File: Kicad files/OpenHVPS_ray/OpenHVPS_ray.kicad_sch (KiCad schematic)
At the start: 69 parts, among them J1 Conn_01x03_Male, J2 Conn_01x03_Male, Q1 FQT7N10, Q2 BC846A, Q3 MMDT3906, U1 MAX6008AEUR+T, U2 74HC14, U3 MAX4162, U4 CD14538BM

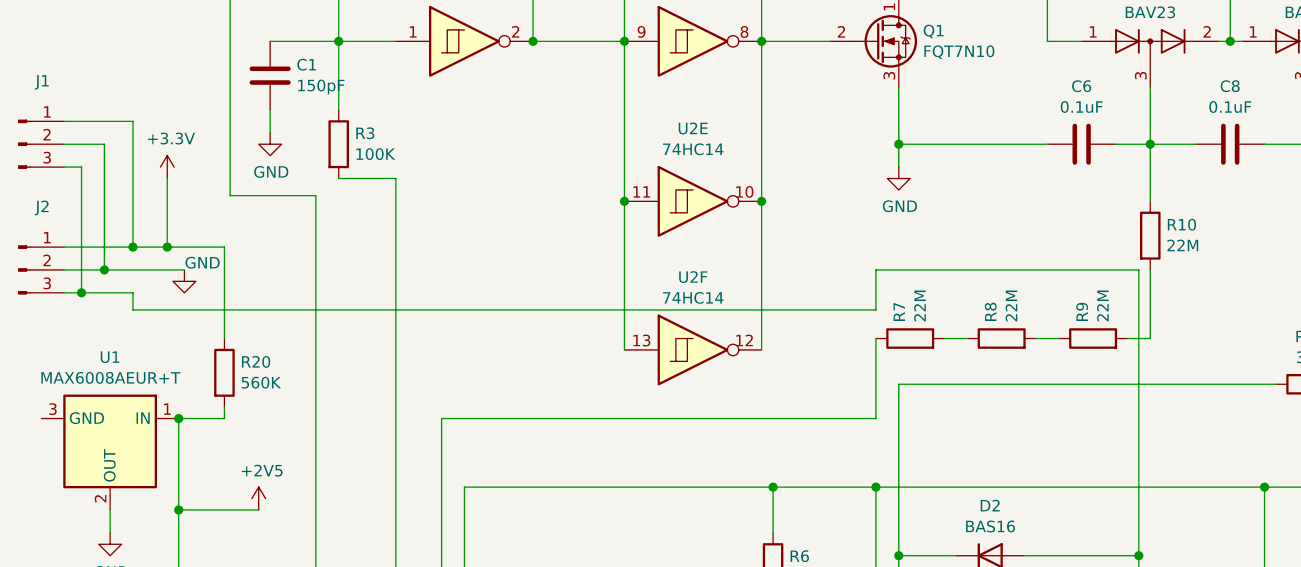
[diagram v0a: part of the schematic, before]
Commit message: Flipped R1 and +-P-GND and naming
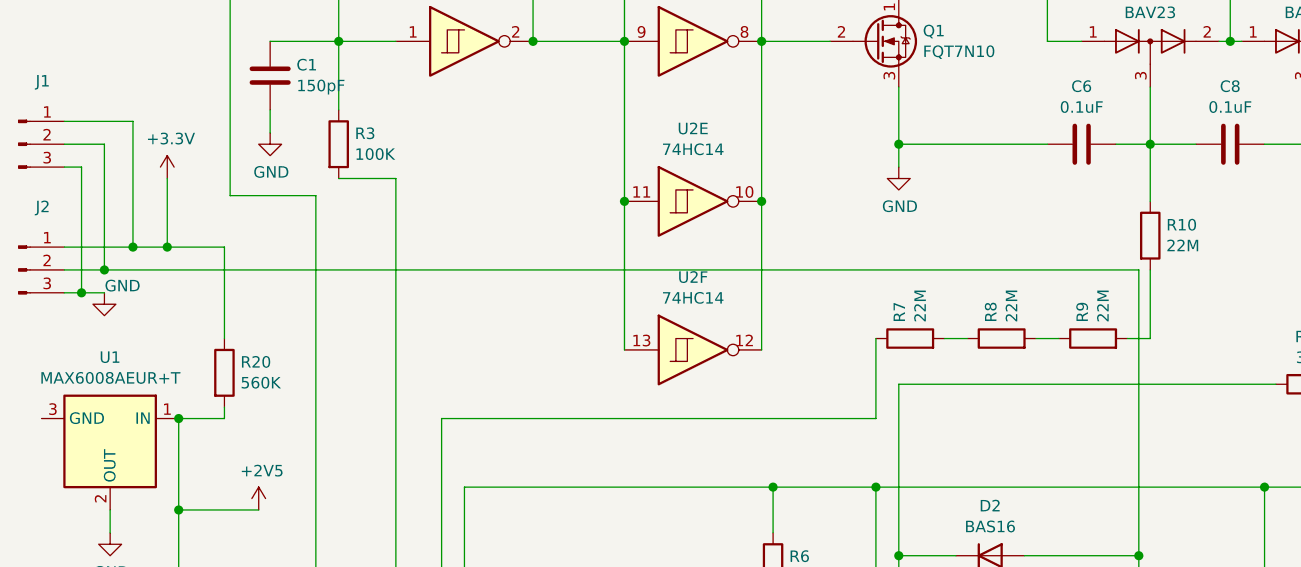
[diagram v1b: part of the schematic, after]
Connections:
- net GND: now also J1.3 (Pin_3), J2.3 (Pin_3); no longer J1.2 (Pin_2), J2.2 (Pin_2)
- net at D2.2 (A), U4.6 (Q): now also J1.2 (Pin_2), J2.2 (Pin_2); no longer J1.3 (Pin_3), J2.3 (Pin_3)
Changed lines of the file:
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@@
     (stroke (width 0) (type solid) (color 0 0 0 0))
   )
-  (wire (pts (xy 24.765 116.205) (xy 30.48 116.205))
+  (wire (pts (xy 24.765 116.205) (xy 27.305 116.205))
     (stroke (width 0) (type solid) (color 0 0 0 0))
   )
@@
     (stroke (width 0) (type solid) (color 0 0 0 0))
   )
-  (wire (pts (xy 27.305 113.665) (xy 36.195 113.665))
+  (wire (pts (xy 27.305 113.665) (xy 142.24 113.665))
     (stroke (width 0) (type solid) (color 0 0 0 0))
   )
@@
     (stroke (width 0) (type solid) (color 0 0 0 0))
   )
-  (wire (pts (xy 30.48 118.11) (xy 30.48 116.205))
-    (stroke (width 0) (type solid) (color 0 0 0 0))
-  )
-  (wire (pts (xy 30.48 118.11) (xy 113.03 118.11))
-    (stroke (width 0) (type solid) (color 0 0 0 0))
-  )
   (wire (pts (xy 30.48 164.465) (xy 30.48 174.625))
     (stroke (width 0) (type solid) (color 0 0 0 0))
@@
   )
   (wire (pts (xy 110.49 177.165) (xy 129.54 177.165))
-    (stroke (width 0) (type solid) (color 0 0 0 0))
-  )
-  (wire (pts (xy 113.03 113.665) (xy 142.24 113.665))
-    (stroke (width 0) (type solid) (color 0 0 0 0))
-  )
-  (wire (pts (xy 113.03 118.11) (xy 113.03 113.665))
     (stroke (width 0) (type solid) (color 0 0 0 0))
   )
@@
     )
   )
+  (symbol (lib_id "power:GND") (at 27.305 116.205 0) (unit 1)
+    (in_bom yes) (on_board yes)
+    (property "Reference" "#PWR05" (id 0) (at 27.305 122.555 0)
+      (effects (font (size 1.27 1.27)) hide)
+    )
+    (property "Value" "GND" (id 1) (at 29.3243 115.4494 0))
+    (property "Footprint" "" (id 2) (at 27.305 116.205 0)
+      (effects (font (size 1.27 1.27)) hide)
+    )
+    (property "Datasheet" "" (id 3) (at 27.305 116.205 0)
+      (effects (font (size 1.27 1.27)) hide)
+    )
+  )
   (symbol (lib_id "power:GND") (at 27.94 142.875 0) (unit 1)
     (in_bom yes) (on_board yes)
@@
       (effects (font (size 1.27 1.27)) hide)
     )
-  )
-  (symbol (lib_id "power:GND") (at 36.195 113.665 0) (unit 1)
-    (in_bom yes) (on_board yes)
-    (property "Reference" "#PWR05" (id 0) (at 36.195 120.015 0)
-      (effects (font (size 1.27 1.27)) hide)
-    )
-    (property "Value" "GND" (id 1) (at 38.2143 112.9094 0))
-    (property "Footprint" "" (id 2) (at 36.195 113.665 0)
-      (effects (font (size 1.27 1.27)) hide)
-    )
-    (property "Datasheet" "" (id 3) (at 36.195 113.665 0)
-      (effects (font (size 1.27 1.27)) hide)
-    )
